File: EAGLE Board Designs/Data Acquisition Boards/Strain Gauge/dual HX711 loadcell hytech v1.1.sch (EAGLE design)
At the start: 48 parts, among them Q1 MMBT4403, Q2 MMBT4403, U1 HX711, U2 HX711, X1 CONNECTOR-6, X2 CONNECTOR-2, X4 CONNECTOR-4, X5 CONNECTOR-4

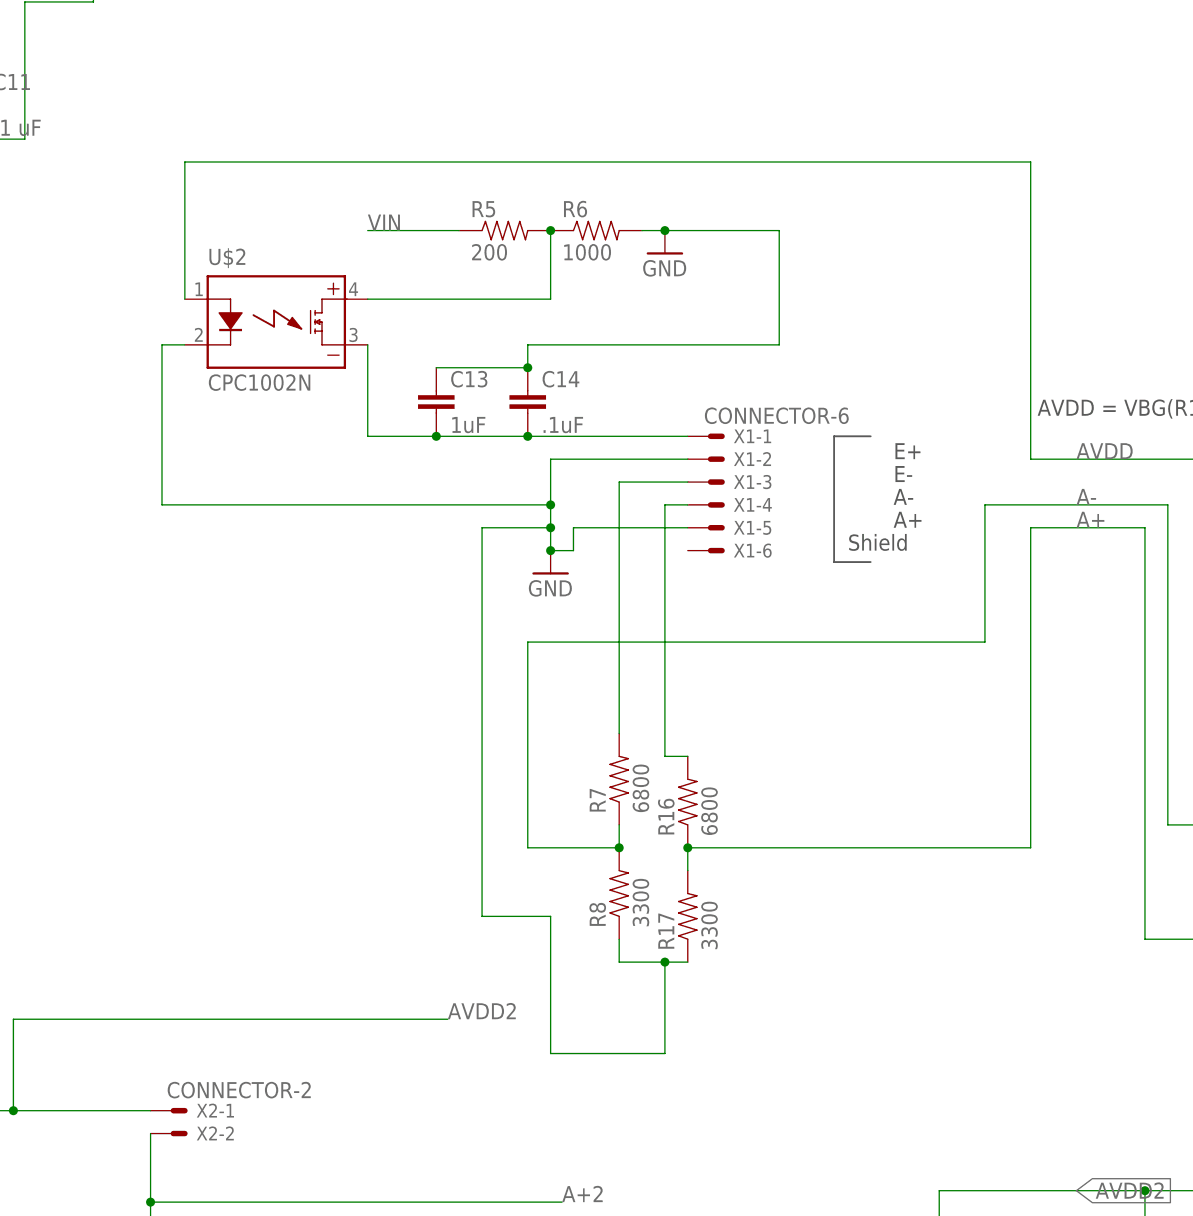
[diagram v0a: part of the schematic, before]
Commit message: v1.1 is designed to use GTMS load cells
GTMS load cells can be excited by the 3.3V output of the HX711 so no complication is neeeded regarding voltage dividers or an optocoupler
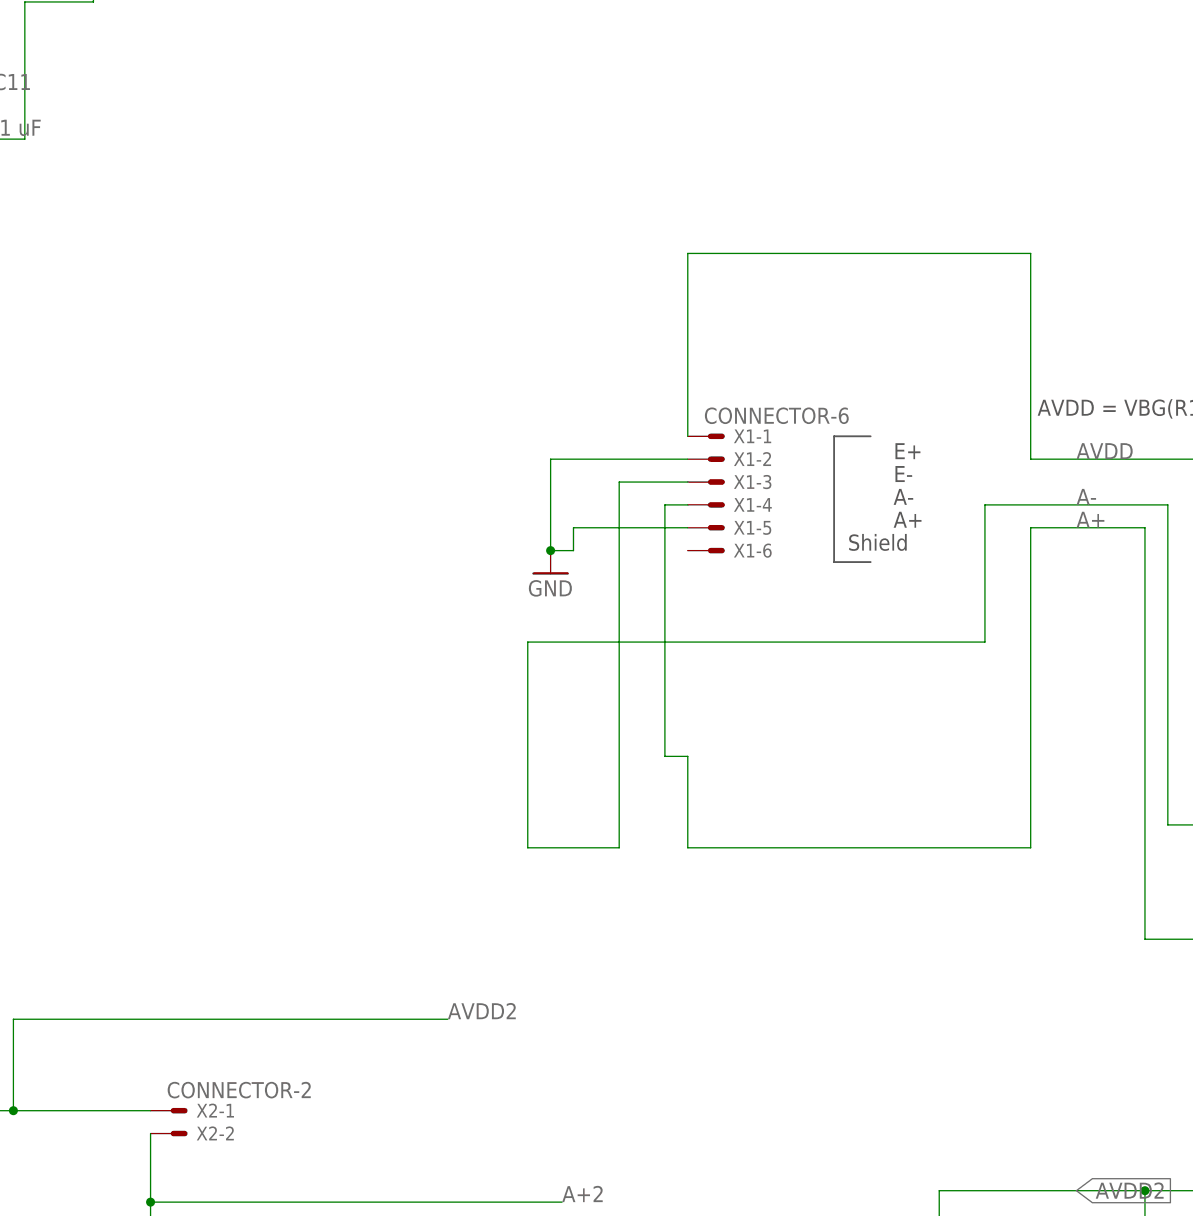
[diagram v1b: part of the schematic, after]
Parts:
- removed C13: 1uF, HyTechDevices:CAP0805
- removed C14: .1uF, HyTechDevices:CAP0805
- removed R16, R7: 6800, HyTechDevices:RESISTORAXIAL-0.3
- removed R17, R8: 3300, HyTechDevices:RESISTORAXIAL-0.3
- removed R5: 200, HyTechDevices:RESISTOR0805-RES
- removed R6: 1000, HyTechDevices:RESISTORAXIAL-0.3
- removed U$2: CPC1002N, HyTechDevices:CPC1002N
- R10, R11, R9: device HyTechDevices:RESISTORAXIAL-0.3 -> HyTechDevices:RESISTOR0805-RES
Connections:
- removed net N$13: R16.2, X1-4.S
- removed net N$14: C13.2, C14.2, U$2.DC-, X1-1.S
- removed net N$15: R5.2, R6.1, U$2.DC+
- removed net N$16: R7.2, X1-3.S
- net A+: now also X1-4.S; no longer R16.1, R17.2
- net A-: now also X1-3.S; no longer R7.1, R8.2
- net AVDD: now also X1-1.S; no longer U$2.CONTROL+
- net GND: no longer C13.1, C14.1, R17.1, R6.2, R8.1, U$2.CONTROL-
- net VIN: no longer R5.1
